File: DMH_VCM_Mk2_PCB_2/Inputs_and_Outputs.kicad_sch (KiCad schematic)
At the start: 36 parts, among them J0 Conn_01x01, J1 TS_Jack_6.35mm_Sw, J10 TS_Jack_6.35mm_Sw, J2 TS_Jack_6.35mm_Sw, J200 IDC_02x05, J3 TS_Jack_6.35mm_Sw, J4 TS_Jack_6.35mm_Sw, J5 TS_Jack_6.35mm_Sw, J50 Conn_01x08, J6 TS_Jack_6.35mm_Sw, J60 Conn_01x08, J7 TS_Jack_6.35mm_Sw, J70 Conn_01x08, J8 TS_Jack_6.35mm_Sw, J9 TS_Jack_6.35mm_Sw, SW1 SW_DPDT, SW2 SW_DPDT, SW3 SW_DPDT

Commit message: Positioned PCB 2 components
Volume conflict with headers, needs correction o PCB 1
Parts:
- J50, J60, J70: footprint Connector_PinSocket_2.54mm:PinSocket_1x08_P2.54mm_Vertical -> Connector_PinHeader_2.54mm:PinHeader_1x08_P2.54mm_Vertical
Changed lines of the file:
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@@
 		(exclude_from_sim no)
 		(in_bom yes)
-		(on_board yes)
+		(on_board no)
 		(dnp no)
 		(property "Reference" "J9"
@@
 		(exclude_from_sim no)
 		(in_bom yes)
-		(on_board yes)
+		(on_board no)
 		(dnp no)
 		(property "Reference" "J2"
@@
 		(exclude_from_sim no)
 		(in_bom yes)
-		(on_board no)
+		(on_board yes)
 		(dnp no)
 		(property "Reference" "D4"
@@
 		(exclude_from_sim no)
 		(in_bom yes)
-		(on_board no)
+		(on_board yes)
 		(dnp no)
 		(property "Reference" "SW1"
@@
 		(exclude_from_sim no)
 		(in_bom yes)
-		(on_board no)
+		(on_board yes)
 		(dnp no)
 		(property "Reference" "SW3"
@@
 		(exclude_from_sim no)
 		(in_bom yes)
-		(on_board yes)
+		(on_board no)
 		(dnp no)
 		(fields_autoplaced yes)
@@
 		(exclude_from_sim no)
 		(in_bom yes)
-		(on_board no)
+		(on_board yes)
 		(dnp no)
 		(fields_autoplaced yes)
@@
 		(exclude_from_sim no)
 		(in_bom yes)
-		(on_board no)
+		(on_board yes)
 		(dnp no)
 		(property "Reference" "RV5"
@@
 		(exclude_from_sim no)
 		(in_bom yes)
-		(on_board yes)
+		(on_board no)
 		(dnp no)
 		(property "Reference" "J5"
@@
 		(exclude_from_sim no)
 		(in_bom yes)
-		(on_board no)
+		(on_board yes)
 		(dnp no)
 		(property "Reference" "RV7"
@@
 		(exclude_from_sim no)
 		(in_bom yes)
-		(on_board yes)
+		(on_board no)
 		(dnp no)
 		(property "Reference" "J4"
@@
 		(exclude_from_sim no)
 		(in_bom yes)
-		(on_board yes)
+		(on_board no)
 		(dnp no)
 		(property "Reference" "J10"
@@
 		(exclude_from_sim no)
 		(in_bom yes)
-		(on_board no)
+		(on_board yes)
 		(dnp no)
 		(property "Reference" "SW2"
@@
 		(exclude_from_sim no)
 		(in_bom yes)
-		(on_board yes)
+		(on_board no)
 		(dnp no)
 		(property "Reference" "J7"
@@
 		(exclude_from_sim no)
 		(in_bom yes)
-		(on_board yes)
+		(on_board no)
 		(dnp no)
 		(property "Reference" "J8"
@@
 		(exclude_from_sim no)
 		(in_bom yes)
-		(on_board no)
+		(on_board yes)
 		(dnp no)
 		(fields_autoplaced yes)
@@
 		(exclude_from_sim no)
 		(in_bom yes)
-		(on_board no)
+		(on_board yes)
 		(dnp no)
 		(property "Reference" "RV8"
@@
 		(exclude_from_sim no)
 		(in_bom yes)
-		(on_board no)
+		(on_board yes)
 		(dnp no)
 		(property "Reference" "RV9"
@@
 		(exclude_from_sim no)
 		(in_bom yes)
-		(on_board no)
+		(on_board yes)
 		(dnp no)
 		(property "Reference" "D3"
@@
 		(exclude_from_sim no)
 		(in_bom yes)
-		(on_board no)
+		(on_board yes)
 		(dnp no)
 		(fields_autoplaced yes)
@@
 		(exclude_from_sim no)
 		(in_bom yes)
-		(on_board no)
+		(on_board yes)
 		(dnp no)
 		(property "Reference" "RV4"
@@
 			)
 		)
-		(property "Footprint" "Connector_PinSocket_2.54mm:PinSocket_1x08_P2.54mm_Vertical"
+		(property "Footprint" "Connector_PinHeader_2.54mm:PinHeader_1x08_P2.54mm_Vertical"
 			(at 127 115.57 0)
 			(effects
@@
 		(exclude_from_sim no)
 		(in_bom yes)
-		(on_board no)
+		(on_board yes)
 		(dnp no)
 		(property "Reference" "D5"
@@
 			)
 		)
-		(property "Footprint" "Connector_PinSocket_2.54mm:PinSocket_1x08_P2.54mm_Vertical"
+		(property "Footprint" "Connector_PinHeader_2.54mm:PinHeader_1x08_P2.54mm_Vertical"
 			(at 127 191.77 0)
 			(effects
@@
 			)
 		)
-		(property "Footprint" "Connector_PinSocket_2.54mm:PinSocket_1x08_P2.54mm_Vertical"
+		(property "Footprint" "Connector_PinHeader_2.54mm:PinHeader_1x08_P2.54mm_Vertical"
 			(at 127 39.37 0)
 			(effects
@@
 		(exclude_from_sim no)
 		(in_bom yes)
-		(on_board no)
+		(on_board yes)
 		(dnp no)
 		(fields_autoplaced yes)
@@
 		(exclude_from_sim no)
 		(in_bom yes)
-		(on_board yes)
+		(on_board no)
 		(dnp no)
 		(property "Reference" "J3"
@@
 		(exclude_from_sim no)
 		(in_bom yes)
-		(on_board no)
+		(on_board yes)
 		(dnp no)
 		(property "Reference" "R61"
@@
 		(exclude_from_sim no)
 		(in_bom yes)
-		(on_board no)
+		(on_board yes)
 		(dnp no)
 		(property "Reference" "RV6"
@@
 		(exclude_from_sim no)
 		(in_bom no)
-		(on_board no)
+		(on_board yes)
 		(dnp yes)
 		(property "Reference" "J0"
@@
 		(exclude_from_sim no)
 		(in_bom yes)
-		(on_board no)
+		(on_board yes)
 		(dnp no)
 		(property "Reference" "R57"
@@
 		(exclude_from_sim no)
 		(in_bom yes)
-		(on_board yes)
+		(on_board no)
 		(dnp no)
 		(property "Reference" "J1"
@@
 		(exclude_from_sim no)
 		(in_bom yes)
-		(on_board yes)
+		(on_board no)
 		(dnp no)
 		(property "Reference" "J6"
@@
 		(exclude_from_sim no)
 		(in_bom yes)
-		(on_board no)
+		(on_board yes)
 		(dnp no)
 		(fields_autoplaced yes)
@@
 		(exclude_from_sim no)
 		(in_bom yes)
-		(on_board no)
+		(on_board yes)
 		(dnp no)
 		(fields_autoplaced yes)
@@
 		(exclude_from_sim no)
 		(in_bom yes)
-		(on_board no)
+		(on_board yes)
 		(dnp no)
 		(property "Reference" "R59"

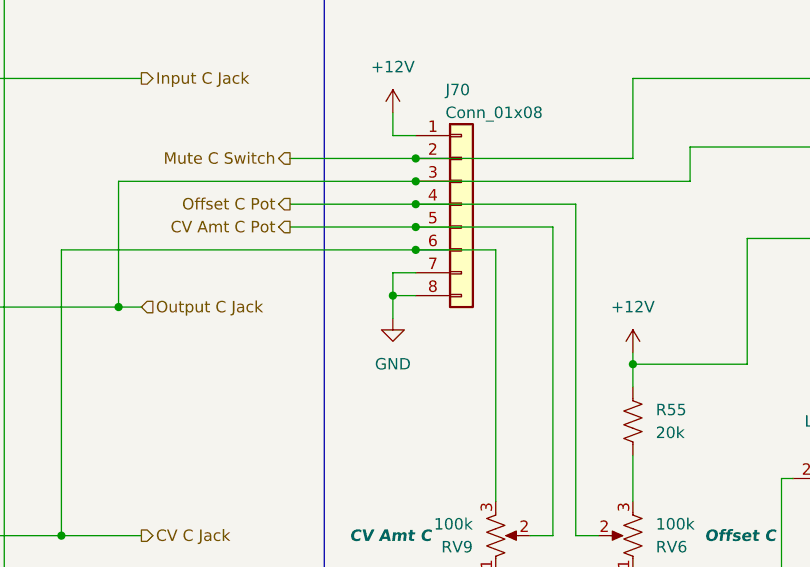
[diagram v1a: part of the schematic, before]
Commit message: Resolved J70 volume conflict
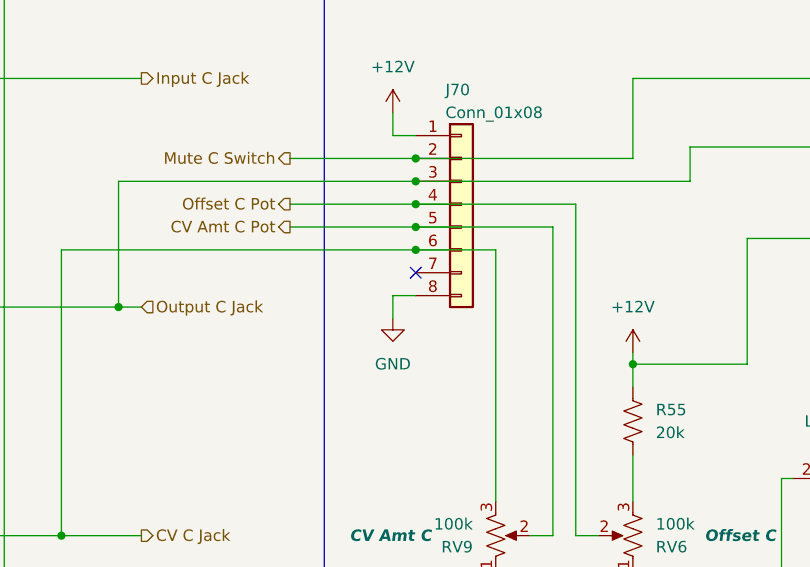
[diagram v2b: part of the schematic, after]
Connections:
- net GND: no longer J70.7 (Pin_7)
- no-connect marks 3 -> 4
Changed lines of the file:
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@@
-	)
-	(junction
-		(at 119.38 201.93)
-		(diameter 0)
-		(color 0 0 0 0)
 	)
 	(junction
@@
 		(diameter 0)
 		(color 0 0 0 0)
+	)
+	(no_connect
+		(at 121.92 199.39)
 	)
 	(no_connect
@@
 	(wire
 		(pts
-			(xy 119.38 199.39) (xy 119.38 201.93)
-		)
-		(stroke
-			(width 0)
-			(type default)
-		)
-	)
-	(wire
-		(pts
 			(xy 119.38 184.15) (xy 121.92 184.15)
 		)
@@
 		)
 		(stroke
-			(width 0)
-			(type default)
-		)
-	)
-	(wire
-		(pts
-			(xy 121.92 199.39) (xy 119.38 199.39)
-		)
-		(stroke

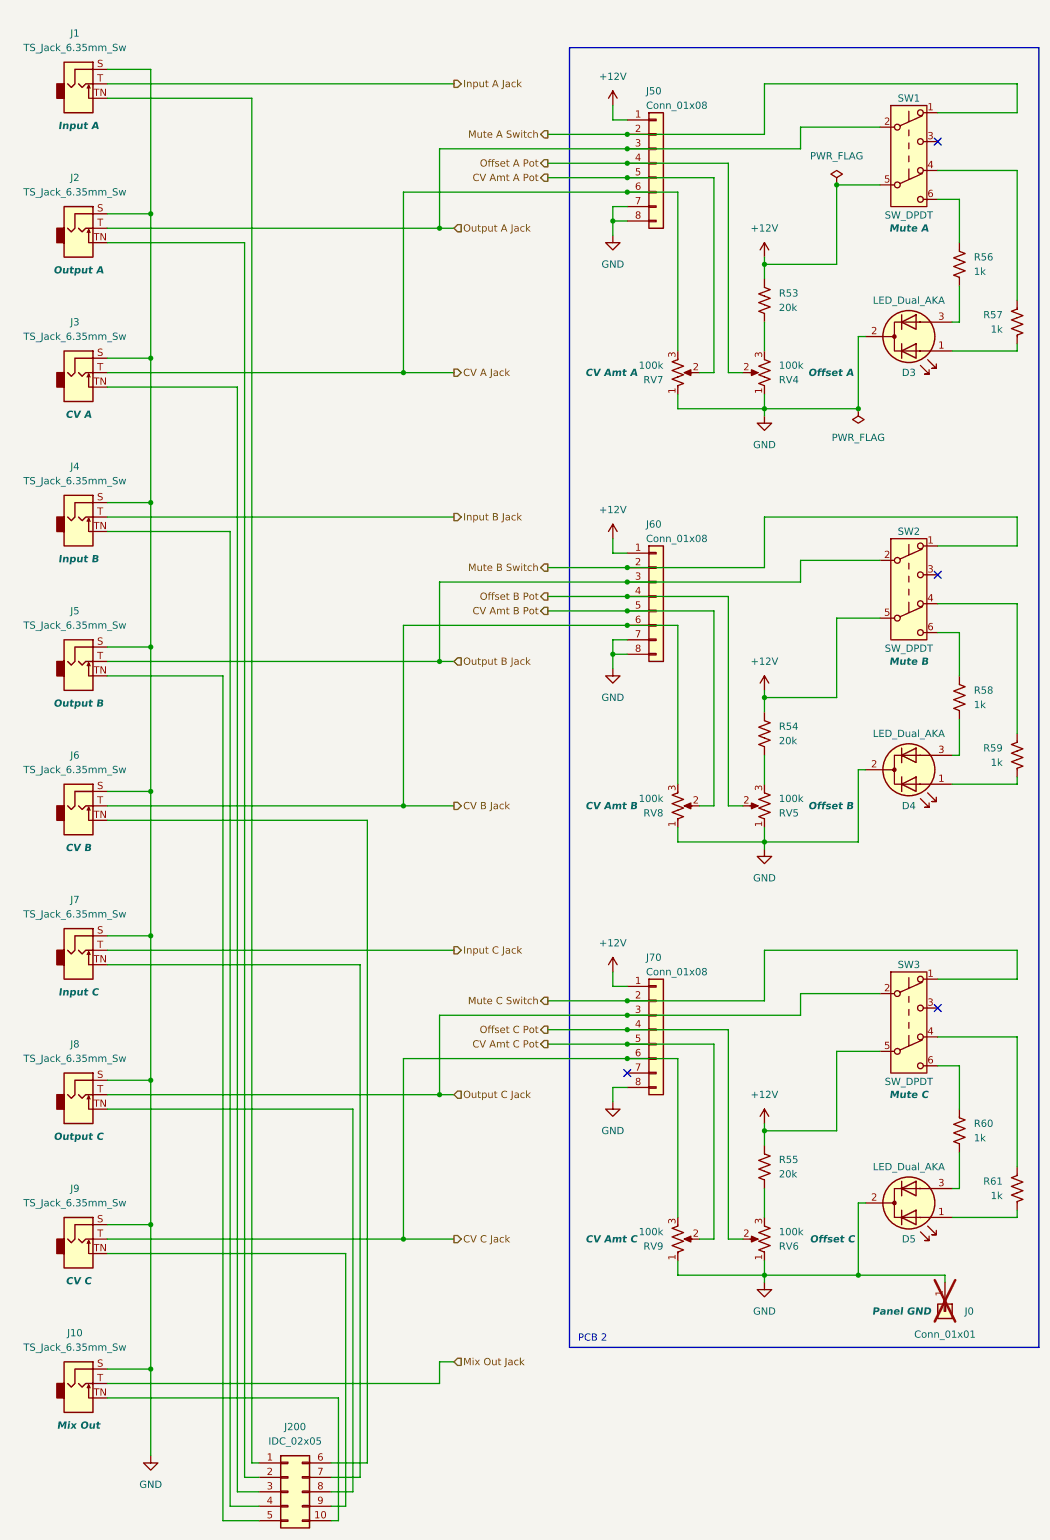
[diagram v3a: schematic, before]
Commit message: Added +/-7v5 to input TN and normalled CV inputs
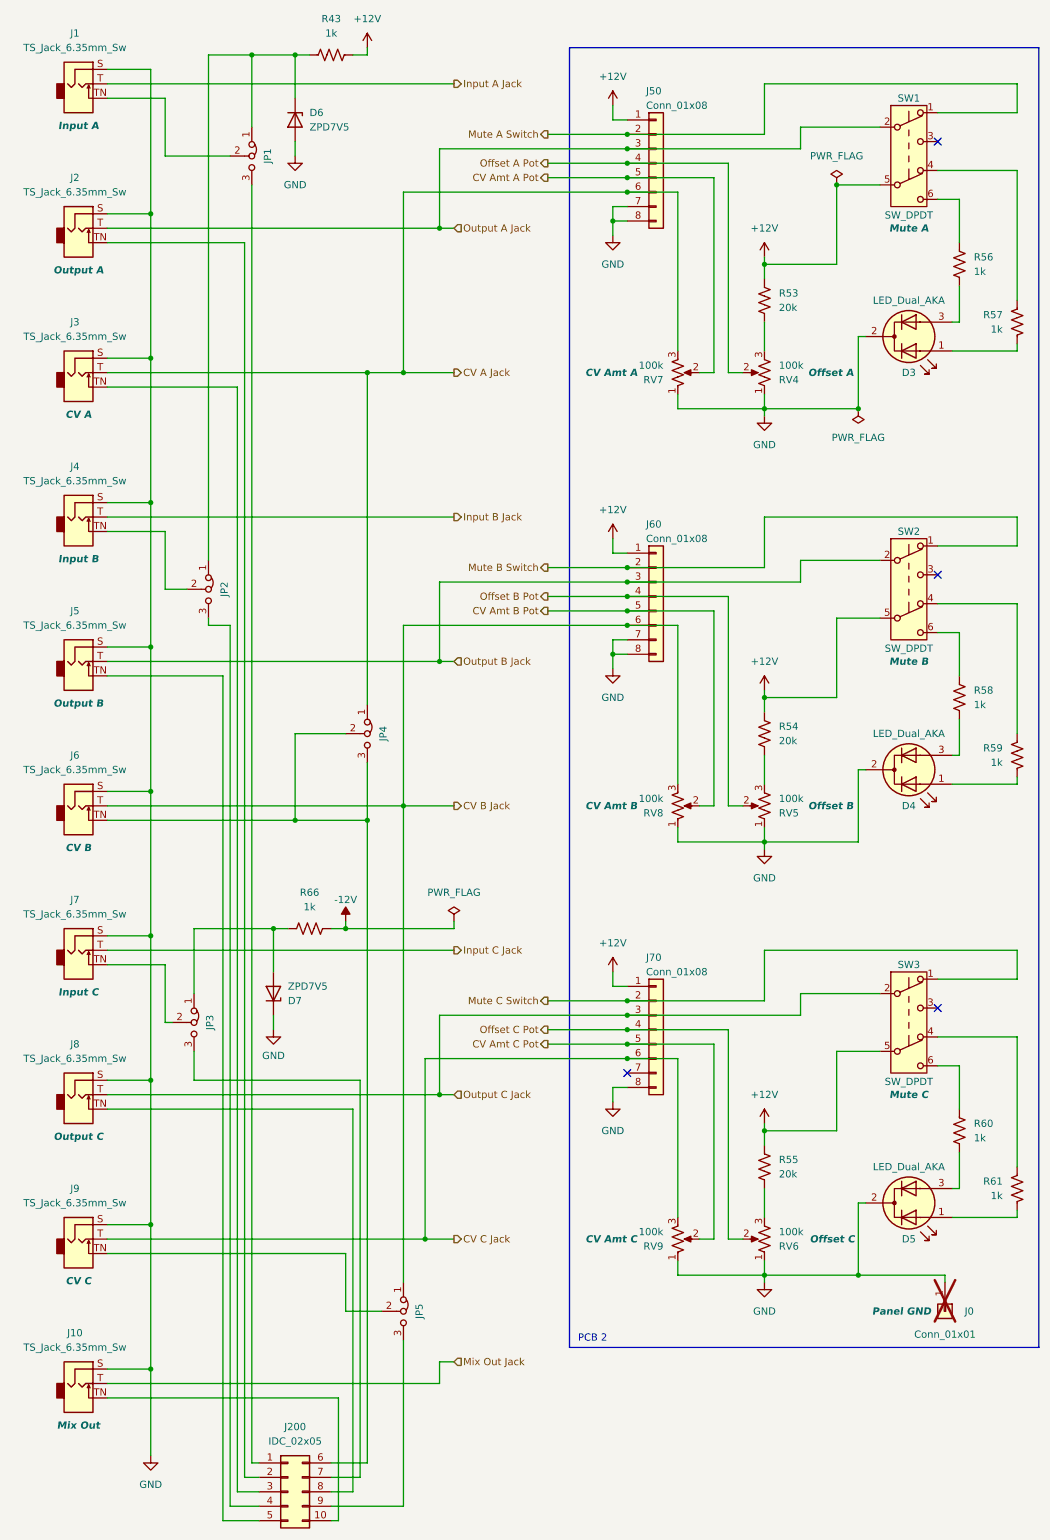
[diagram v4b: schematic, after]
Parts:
- added D6, D7: ZPD7V5, Diode_THT:D_DO-35_SOD27_P7.62mm_Horizontal, symbol Diode:ZPDxx
- added JP1, JP2, JP3, JP4, JP5: Jumper_3_Bridged12, Connector_PinHeader_2.54mm:PinHeader_1x03_P2.54mm_Vertical, symbol Jumper:Jumper_3_Bridged12
- added R43, R66: 1k, Resistor_THT:R_Axial_DIN0207_L6.3mm_D2.5mm_P2.54mm_Vertical, symbol Device:R_US
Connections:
- net +12V: now also R43.1
- net CV A Jack: now also JP4.1 (A)
- net CV B Jack: now also JP5.1 (A)
- net GND: now also D6.2 (A), D7.1 (K)
- net at J9.TN: now also JP5.2 (C); no longer J200.9 (Pin_9)
- net at J200.1 (Pin_1): now also JP1.3 (B); no longer J1.TN
- net at J200.4 (Pin_4): now also JP2.3 (B); no longer J4.TN
- net at J200.6 (Pin_6), J6.TN: now also JP4.2 (C), JP4.3 (B)
- net at J200.7 (Pin_7): now also JP3.3 (B); no longer J7.TN
- new net: J200.9 (Pin_9), JP5.3 (B)
- new net: J4.TN, JP2.2 (C)
- new net: J7.TN, JP3.2 (C)
- new net: D6.1 (K), JP1.1 (A), JP2.1 (A), R43.2
- new net: J1.TN, JP1.2 (C)
- new net: D7.2 (A), JP3.1 (A), R66.2
- new net -12V: R66.1
